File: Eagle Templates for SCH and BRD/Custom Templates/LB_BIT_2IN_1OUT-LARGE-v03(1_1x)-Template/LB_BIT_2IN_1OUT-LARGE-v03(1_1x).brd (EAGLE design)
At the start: 21.6 x 26.9 mm, 23 parts, among them U1 LV321SOT23-5, U2 LV321SOT23-5, U6 LV321SOT23-5

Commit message: added bitlab logo and made minor changes to board templates. Updated littlebits library.
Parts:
- added U$3: (no value), LITTLEBITS:BITLAB-LOGO
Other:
- board text added: "iX Name Here"
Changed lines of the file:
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@@
 <text x="21.2" y="-6.8" size="1" layer="52" rot="MR0">W15-NOR BOTTOM</text>
 <dimension x1="3.005" y1="4.62" x2="3.005" y2="9.12" x3="-11.65" y3="6.87" textsize="1.778" layer="47"/>
+<text x="20.3" y="22.9" size="1.3" layer="21" font="vector" rot="SR270" align="center">iX Name Here</text>
 </plain>
 <attributes>
@@
 <element name="U$1" library="LITTLEBITS" package="OSHWCREDIT" value="OSHWCREDIT" x="-94.24" y="-62.425"/>
 <element name="FRAME1" library="LITTLEBITS" package="FABDWG01-OHW" value="FRAME-LETTER" x="0" y="0"/>
+<element name="U$3" library="LITTLEBITS" package="BITLAB-LOGO" value="" x="18.4" y="26" rot="R270"/>
 </elements>
 <signals>

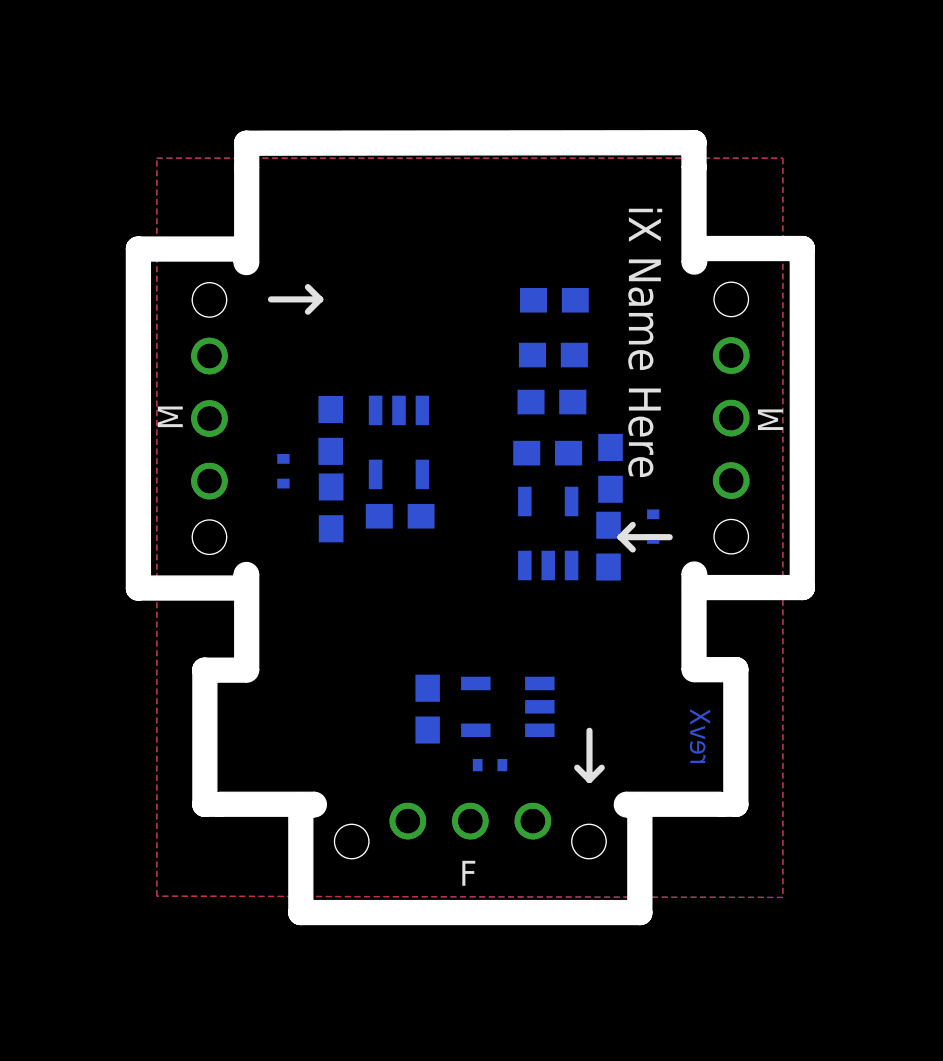
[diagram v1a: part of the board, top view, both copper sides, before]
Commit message: Updated templates
- Added ferrite beads
- Moved text and annotations off of Nets layer
- Minor layout changes
- Removed I/O/W prefix from reference designators
- Removed output stage components from output bits
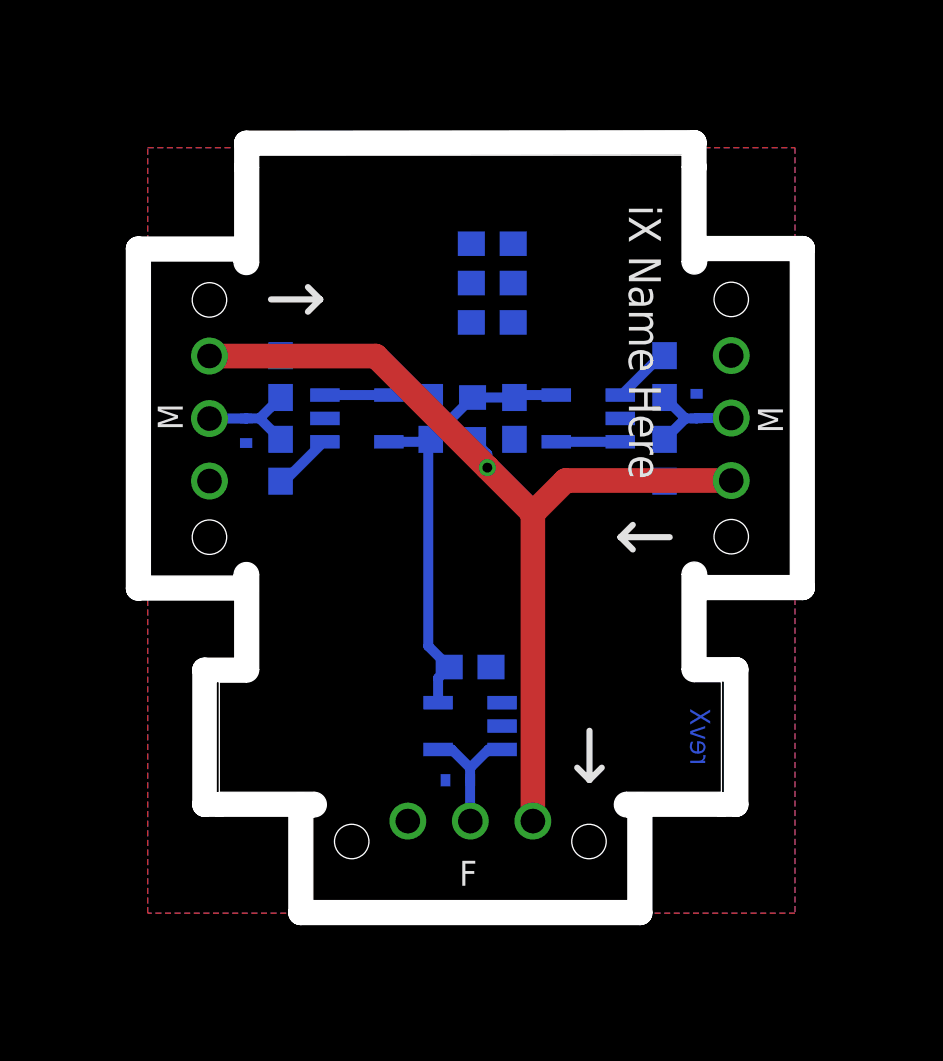
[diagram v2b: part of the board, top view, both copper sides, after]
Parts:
- removed I?C1, I?C3: 0.1uF, LITTLEBITS:CAP-0603
- removed I?C2: 10uF, LITTLEBITS:CAP-0603
- removed I?C4: 1.0uF, LITTLEBITS:CAP-0603
- removed I?R1, I?R5: 1meg, LITTLEBITS:RES-0603
- removed I?R2, I?R6: 10K, LITTLEBITS:RES-0603
- removed I?R3, I?R4: 3K3, LITTLEBITS:RES-0603
- removed I?TVS1, I?TVS2, I?TVS6: ESD9B5.0ST5G, LITTLEBITS:SOD-923
- removed U6: LV321SOT23-5, LITTLEBITS:SOT23-5
- added C1, C3: 0.1uF, LITTLEBITS:CAP-0603
- added C2: 10uF, LITTLEBITS:CAP-0603
- added C4: 1.0uF, LITTLEBITS:CAP-0603
- added FB1: FERRITE-BEAD0603, LITTLEBITS:R0603
- added R1, R5: 1meg, LITTLEBITS:RES-0603
- added R2, R6: 10K, LITTLEBITS:RES-0603
- added R3, R4: 3K3, LITTLEBITS:RES-0603
- added TVS1, TVS2, TVS3: ESD9B5.0ST5G, LITTLEBITS:SOD-923
- added U3: LV321SOT23-5, LITTLEBITS:SOT23-5
- moved U1 4.95 mm to (18.0, 19.8), turned to 270 degrees
- moved U2 1.97 mm to (8.60, 19.8), turned to 90 degrees
- renumbered W15BSF1 to BSF1, W15BSM1 to BSM1, W15BSM2 to BSM2
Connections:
- new net LB_VCC: BSF1.VCC, BSM1.VCC1, BSM2.VCC1, FB1.2
- new net SIG_IN1: BSM1.SIG1, R1.2, R2.2, TVS1.2
- new net SIG_IN2: BSM2.SIG1, R5.2, R6.2, TVS2.2
- net GND: now also C1.2, C2.2, C3.2, C4.1, R1.1, R4.1, R5.1, TVS1.1, TVS2.1, TVS3.1, U3.2; no longer I?C1.2, I?C2.2, I?C3.2, I?C4.1, I?R1.1, I?R4.1, I?R5.1, I?TVS1.1, I?TVS2.1, I?TVS6.1, U6.2
- net N$12: now also U3.1; no longer U6.1
- net N$2: now also R6.1; no longer I?R6.1
- net N$4: now also R2.1; no longer I?R2.1
- net SIG_OUT: now also BSF1.SIG, TVS3.2, U3.3, U3.4; no longer BSM1.SIG1, BSM2.SIG1, I?R1.2, I?R2.2, I?R5.2, I?R6.2, I?TVS1.2, I?TVS2.2, I?TVS6.2, U6.3, U6.4
- net VCC: now also C1.1, C3.1, C4.2, FB1.1, R3.2, U3.5; no longer BSF1.VCC, BSM1.VCC1, BSM2.VCC1, I?C1.1, I?C3.1, I?C4.2, I?R3.2, U6.5
- net VREF: now also C2.1, R3.1, R4.2; no longer I?C2.1, I?R3.1, I?R4.2
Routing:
- net LB_VCC: track 0.00 -> 38.3 mm, vias 0 -> 1
- net VCC: track 0.00 -> 18.7 mm
- net SIG_OUT: track 0.00 -> 5.39 mm
- net SIG_IN2: track 0.00 -> 4.45 mm
- net SIG_IN1: track 0.00 -> 4.27 mm
- net N$3: track 0.00 -> 2.60 mm
- net N$1: track 0.00 -> 2.60 mm
- net N$4: track 0.00 -> 2.46 mm
- net N$2: track 0.00 -> 2.46 mm
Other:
- outline, holes or cut-outs redrawn
- board text removed: "LARGE"
- board text removed: "W15-NOR BOTTOM"
- board text removed: "W15-NOR TOP"
- board text removed: "W15BSF1 (ORANGE)"
- board text removed: "W15BSM1 (ORANGE)"
- board text removed: "W15BSM2 (ORANGE)"
